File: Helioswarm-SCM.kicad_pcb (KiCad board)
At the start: 8 copper layers, 78 x 38 mm, 102 parts, among them J404 DB25_Female_MountingHoles, J405 DB15_Male_MountingHoles, U1 ASIC_JUICE

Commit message: Simplified schematic and reset(cleared) PCB
Signed-off-by: Alexis Jeandet <alexis.jeandet@member.fsf.org>
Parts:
- removed CX1, CX2, CX4, CY1, CY2, CY3, CZ1, CZ2, CZ3: 680n, Capacitor_SMD:C_1812_4532Metric_Pad1.30x3.40mm_HandSolder
- removed CX10, CX12, CY10, CY12, CZ10, CZ12: 221p, Capacitor_SMD:C_0603_1608Metric
- removed CX11, CX40, CY11, CY40, CZ11, CZ40: 220n, Capacitor_SMD:C_1206_3216Metric
- removed CX13, CY13, CZ13: 470nF, Capacitor_SMD:C_1210_3225Metric
- removed CX14, CY14, CZ14: 470n, Capacitor_SMD:C_1812_4532Metric_Pad1.30x3.40mm_HandSolder
- removed CX20, CX35, CX36, CX_SC1, CX_SC2, CY20, CY35, CY36, CY_SC1, CY_SC2, CZ20, CZ35, CZ36, CZ_SC1, CZ_SC2: *, Capacitor_SMD:C_0603_1608Metric
- removed CX42, CY42, CZ42: *, Capacitor_SMD:C_0805_2012Metric
- removed CX8, CY8, CZ8: 1n, Capacitor_SMD:C_0603_1608Metric
- removed CX_CR1, CY_CR1, CZ_CR1: 150pF, Capacitor_SMD:C_0603_1608Metric
- removed H1, H2: MountingHole, LibPersoNadj:MountingHole_4.2
- removed J404: DB25_Female_MountingHoles, LibPersoNadj:GMR7580-25S-1BPN
- removed J405: DB15_Male_MountingHoles, LibPersoNadj:GMR7580-15P-1BPN
- removed N_CFP64: Housing_Pad, TestPoint:TestPoint_Pad_2.0x2.0mm
- removed R1: 10k, Resistor_SMD:R_0603_1608Metric
- removed R40: c-c, Resistor_SMD:R_0805_2012Metric_Pad1.15x1.40mm_HandSolder
- removed RX10, RY10, RZ10: 22,1k, Resistor_SMD:R_0603_1608Metric
- removed RX12, RY12, RZ12: 44,2k, Resistor_SMD:R_0603_1608Metric
- removed RX14, RY14, RZ14: 400, Resistor_SMD:R_0603_1608Metric
- removed RX20, RY20, RZ20: 150k, Resistor_SMD:R_0805_2012Metric_Pad1.15x1.40mm_HandSolder
- removed RX30, RY30, RZ30: 7,68k, Resistor_SMD:R_0603_1608Metric
- removed RX31, RX33, RY31, RY33, RZ31, RZ33: 49,9k, Resistor_SMD:R_0603_1608Metric
- removed RX32, RX34, RY32, RY34, RZ32, RZ34: TBD, Resistor_SMD:R_0603_1608Metric
- removed RX35, RX36, RY35, RY36, RZ35, RZ36: 49,9, Resistor_SMD:R_0603_1608Metric
- removed RX40, RY40, RZ40: 750k, Resistor_SMD:R_1206_3216Metric
- removed RX41, RY41, RZ41: 24,9k, Resistor_SMD:R_0603_1608Metric
- removed RX42, RY42, RZ42: 42,2k, Resistor_SMD:R_0603_1608Metric
- removed RthB0: 1k, Resistor_SMD:R_0805_2012Metric_Pad1.15x1.40mm_HandSolder
- removed U1: ASIC_JUICE, LibPersoNadj:ASIC_Juice_CQFP-64
- added C201: *, Capacitor_SMD:C_0603_1608Metric, F.Cu at (110.7, 97.5)
- added C202: *, Capacitor_SMD:C_0603_1608Metric, F.Cu at (124.8, 90.1)
- added C203: *, Capacitor_SMD:C_0603_1608Metric, F.Cu at (116.3, 94.8)
- added C204: *, Capacitor_SMD:C_0603_1608Metric, F.Cu at (110.7, 100.1)
- added C205: *, Capacitor_SMD:C_0603_1608Metric, F.Cu at (120.8, 91.8)
- added C206: *, Capacitor_SMD:C_0603_1608Metric, F.Cu at (114.7, 97.5)
- added C207: 220n, Capacitor_SMD:C_1206_3216Metric, F.Cu at (111.5, 88.0)
- added C208: *, Capacitor_SMD:C_0805_2012Metric, F.Cu at (116.5, 92.1)
- added C212: 1n, Capacitor_SMD:C_0603_1608Metric, F.Cu at (126.0, 87.6)
- added C213: 221p, Capacitor_SMD:C_0603_1608Metric, F.Cu at (120.3, 94.8)
- added C214: 221p, Capacitor_SMD:C_0603_1608Metric, F.Cu at (114.7, 100.1)
- added C215: 220n, Capacitor_SMD:C_1206_3216Metric, F.Cu at (111.5, 91.3)
- added C216: 470nF, Capacitor_SMD:C_1210_3225Metric, F.Cu at (117.1, 88.4)
- added C301: *, Capacitor_SMD:C_0603_1608Metric, F.Cu at (110.7, 117.3)
- added C302: *, Capacitor_SMD:C_0603_1608Metric, F.Cu at (130.0, 106.4)
- added C303: *, Capacitor_SMD:C_0603_1608Metric, F.Cu at (116.3, 114.0)
- added C304: *, Capacitor_SMD:C_0603_1608Metric, F.Cu at (124.8, 108.9)
- added C305: *, Capacitor_SMD:C_0603_1608Metric, F.Cu at (132.8, 111.4)
- added C306: *, Capacitor_SMD:C_0603_1608Metric, F.Cu at (120.3, 112.8)
- added C307: 220n, Capacitor_SMD:C_1206_3216Metric, F.Cu at (117.1, 106.8)
- added C308: *, Capacitor_SMD:C_0805_2012Metric, F.Cu at (116.5, 110.0)
- added C312: 1n, Capacitor_SMD:C_0603_1608Metric, F.Cu at (114.7, 117.3)
- added C313: 221p, Capacitor_SMD:C_0603_1608Metric, F.Cu at (126.0, 106.4)
- added C314: 221p, Capacitor_SMD:C_0603_1608Metric, F.Cu at (120.8, 109.8)
- added C315: 220n, Capacitor_SMD:C_1206_3216Metric, F.Cu at (111.5, 111.1)
- added C316: 470nF, Capacitor_SMD:C_1210_3225Metric, F.Cu at (111.5, 107.3)
- added C401: *, Capacitor_SMD:C_0603_1608Metric, F.Cu at (145.9, 97.5)
- added C402: *, Capacitor_SMD:C_0603_1608Metric, F.Cu at (151.9, 91.8)
- added C403: *, Capacitor_SMD:C_0603_1608Metric, F.Cu at (141.8, 100.1)
- added C404: *, Capacitor_SMD:C_0603_1608Metric, F.Cu at (147.5, 94.8)
- added C405: *, Capacitor_SMD:C_0603_1608Metric, F.Cu at (141.8, 97.5)
- added C406: *, Capacitor_SMD:C_0603_1608Metric, F.Cu at (157.9, 95.1)
- added C407: 220n, Capacitor_SMD:C_1206_3216Metric, F.Cu at (142.7, 88.0)
- added C408: *, Capacitor_SMD:C_0805_2012Metric, F.Cu at (147.7, 92.1)
- added C412: 1n, Capacitor_SMD:C_0603_1608Metric, F.Cu at (157.2, 87.6)
- added C413: 221p, Capacitor_SMD:C_0603_1608Metric, F.Cu at (151.5, 94.8)
- added C414: 221p, Capacitor_SMD:C_0603_1608Metric, F.Cu at (145.9, 100.1)
- added C415: 220n, Capacitor_SMD:C_1206_3216Metric, F.Cu at (142.7, 91.3)
- added C416: 470nF, Capacitor_SMD:C_1210_3225Metric, F.Cu at (148.3, 88.4)
- added H101: MountingHole, LibPersoNadj:MountingHole_4.2, F.Cu at (201.0, 98.5)
- added H102: MountingHole, LibPersoNadj:MountingHole_4.2, F.Cu at (194.8, 109.5)
- added J101: DB15_Male_MountingHoles, LibPersoNadj:GMR7580-15P-1BPN, F.Cu at (176.4, 110.1)
- added J102: DB25_Female_MountingHoles, LibPersoNadj:GMR7580-25S-1BPN, F.Cu at (179.5, 99.1)
- added N_CFP101: Housing_Pad, TestPoint:TestPoint_Pad_2.0x2.0mm, F.Cu at (141.9, 107.2)
- added R101: 10k, Resistor_SMD:R_0603_1608Metric, F.Cu at (145.9, 106.4)
- added R202: 49,9, Resistor_SMD:R_0603_1608Metric, F.Cu at (122.0, 87.6)
- added R203: 7,68k, Resistor_SMD:R_0603_1608Metric, F.Cu at (118.7, 97.3)
- added R204: 49,9k, Resistor_SMD:R_0603_1608Metric, F.Cu at (130.0, 87.6)
- added R205: TBD, Resistor_SMD:R_0603_1608Metric, F.Cu at (124.8, 92.6)
- added R206: 49,9, Resistor_SMD:R_0603_1608Metric, F.Cu at (118.7, 99.8)
- added R207: TBD, Resistor_SMD:R_0603_1608Metric, F.Cu at (128.8, 90.1)
- added R208: 750k, Resistor_SMD:R_1206_3216Metric, F.Cu at (111.5, 94.6)
- added R209: 42,2k, Resistor_SMD:R_0603_1608Metric, F.Cu at (122.7, 97.3)
- added R210: 24,9k, Resistor_SMD:R_0603_1608Metric, F.Cu at (134.0, 87.6)
- added R211: 49,9k, Resistor_SMD:R_0603_1608Metric, F.Cu at (128.8, 92.6)
- added R212: 400, Resistor_SMD:R_0603_1608Metric, F.Cu at (122.7, 99.8)
- added R213: 22,1k, Resistor_SMD:R_0603_1608Metric, F.Cu at (132.8, 90.1)
- added R214: 44,2k, Resistor_SMD:R_0603_1608Metric, F.Cu at (126.7, 95.1)
- added R302: 49,9, Resistor_SMD:R_0603_1608Metric, F.Cu at (124.8, 111.4)
- added R303: 7,68k, Resistor_SMD:R_0603_1608Metric, F.Cu at (122.7, 119.0)
- added R304: 49,9k, Resistor_SMD:R_0603_1608Metric, F.Cu at (128.3, 114.0)
- added R305: TBD, Resistor_SMD:R_0603_1608Metric, F.Cu at (124.3, 116.5)
- added R306: 49,9, Resistor_SMD:R_0603_1608Metric, F.Cu at (132.8, 108.9)
- added R307: TBD, Resistor_SMD:R_0603_1608Metric, F.Cu at (128.8, 111.4)
- added R308: 750k, Resistor_SMD:R_1206_3216Metric, F.Cu at (111.5, 114.4)
- added R309: 42,2k, Resistor_SMD:R_0603_1608Metric, F.Cu at (134.0, 106.4)
- added R310: 24,9k, Resistor_SMD:R_0603_1608Metric, F.Cu at (124.3, 114.0)
- added R311: 49,9k, Resistor_SMD:R_0603_1608Metric, F.Cu at (118.7, 117.8)
- added R312: 400, Resistor_SMD:R_0603_1608Metric, F.Cu at (128.8, 108.9)
- added R313: 22,1k, Resistor_SMD:R_0603_1608Metric, F.Cu at (120.3, 115.3)
- added R314: 44,2k, Resistor_SMD:R_0603_1608Metric, F.Cu at (122.0, 106.4)
- added R402: 49,9, Resistor_SMD:R_0603_1608Metric, F.Cu at (153.1, 87.6)
- added R403: 7,68k, Resistor_SMD:R_0603_1608Metric, F.Cu at (149.9, 97.3)
- added R404: 49,9k, Resistor_SMD:R_0603_1608Metric, F.Cu at (161.2, 87.6)
- added R405: TBD, Resistor_SMD:R_0603_1608Metric, F.Cu at (156.0, 92.6)
- added R406: 49,9, Resistor_SMD:R_0603_1608Metric, F.Cu at (149.9, 99.8)
- added R407: TBD, Resistor_SMD:R_0603_1608Metric, F.Cu at (160.0, 90.1)
- added R408: 750k, Resistor_SMD:R_1206_3216Metric, F.Cu at (142.6, 94.6)
- added R409: 42,2k, Resistor_SMD:R_0603_1608Metric, F.Cu at (153.9, 97.3)
- added R410: 24,9k, Resistor_SMD:R_0603_1608Metric, F.Cu at (165.2, 87.6)
- added R411: 49,9k, Resistor_SMD:R_0603_1608Metric, F.Cu at (160.0, 92.6)
- added R412: 400, Resistor_SMD:R_0603_1608Metric, F.Cu at (153.9, 99.8)
- added R413: 22,1k, Resistor_SMD:R_0603_1608Metric, F.Cu at (164.0, 90.1)
- added R414: 44,2k, Resistor_SMD:R_0603_1608Metric, F.Cu at (156.0, 90.1)
- added U201: ASIC_JUICE, LibPersoNadj:ASIC_Juice_CQFP-64, F.Cu at (172.5, 132.7)
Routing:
- net /Sz: track 71.6 -> 0.00 mm, vias 1 -> 0
- net /+6V_C: track 68.9 -> 0.00 mm, vias 2 -> 0
- net /CAL: track 66.1 -> 0.00 mm, vias 2 -> 0
- net /M_X: track 62.2 -> 0.00 mm, vias 2 -> 0
- net /+6V_B: track 61.7 -> 0.00 mm, vias 2 -> 0
- net /+6V_A: track 55.1 -> 0.00 mm, vias 2 -> 0
- net /M_Y: track 54.2 -> 0.00 mm, vias 2 -> 0
- net /RTNz: track 52.7 -> 0.00 mm, vias 1 -> 0
- net /RTNx: track 50.8 -> 0.00 mm, vias 1 -> 0
- net GND: track 47.7 -> 0.00 mm, vias 38 -> 0
- net /AsicFM/VDD_Y: track 44.0 -> 0.00 mm, vias 3 -> 0
- net /RTNy: track 42.5 -> 0.00 mm, vias 1 -> 0
- net /Sx: track 39.3 -> 0.00 mm, vias 1 -> 0
- net /AsicFM/VDD_X: track 35.1 -> 0.00 mm, vias 2 -> 0
- net /AsicFM/In2P_Y: track 35.0 -> 0.00 mm, vias 2 -> 0
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- removed copper zone on B.Cu, net GND
- removed copper zone on F.Cu, net GND
- removed copper zone on In1.Cu, net GND
- removed copper zone on In2.Cu, net GND
- removed copper zone on In3.Cu, net GND
- removed copper zone on In4.Cu, net GND
- removed copper zone on In5.Cu, net GND
- removed copper zone on In6.Cu, net GND
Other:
- board outline removed

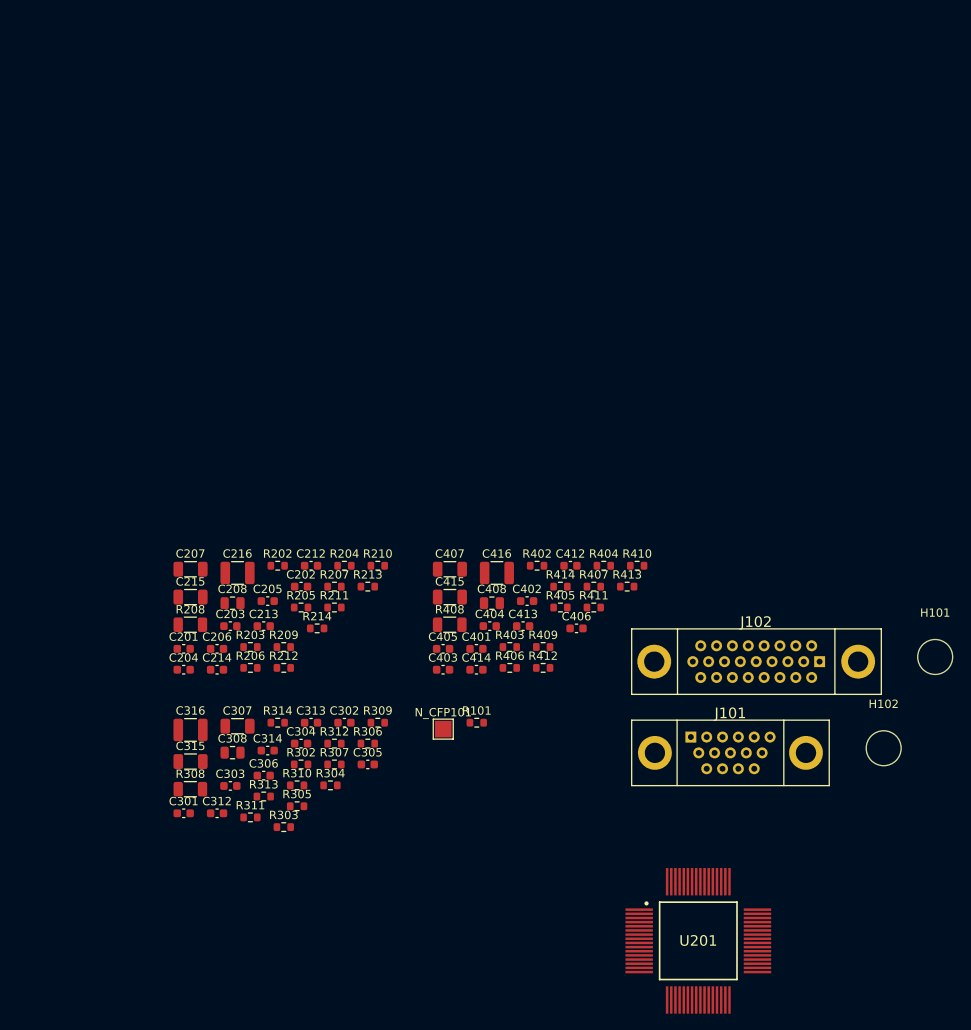
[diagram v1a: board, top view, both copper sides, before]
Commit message: Improved schematic net naming and started layout
Signed-off-by: Alexis Jeandet <alexis.jeandet@member.fsf.org>
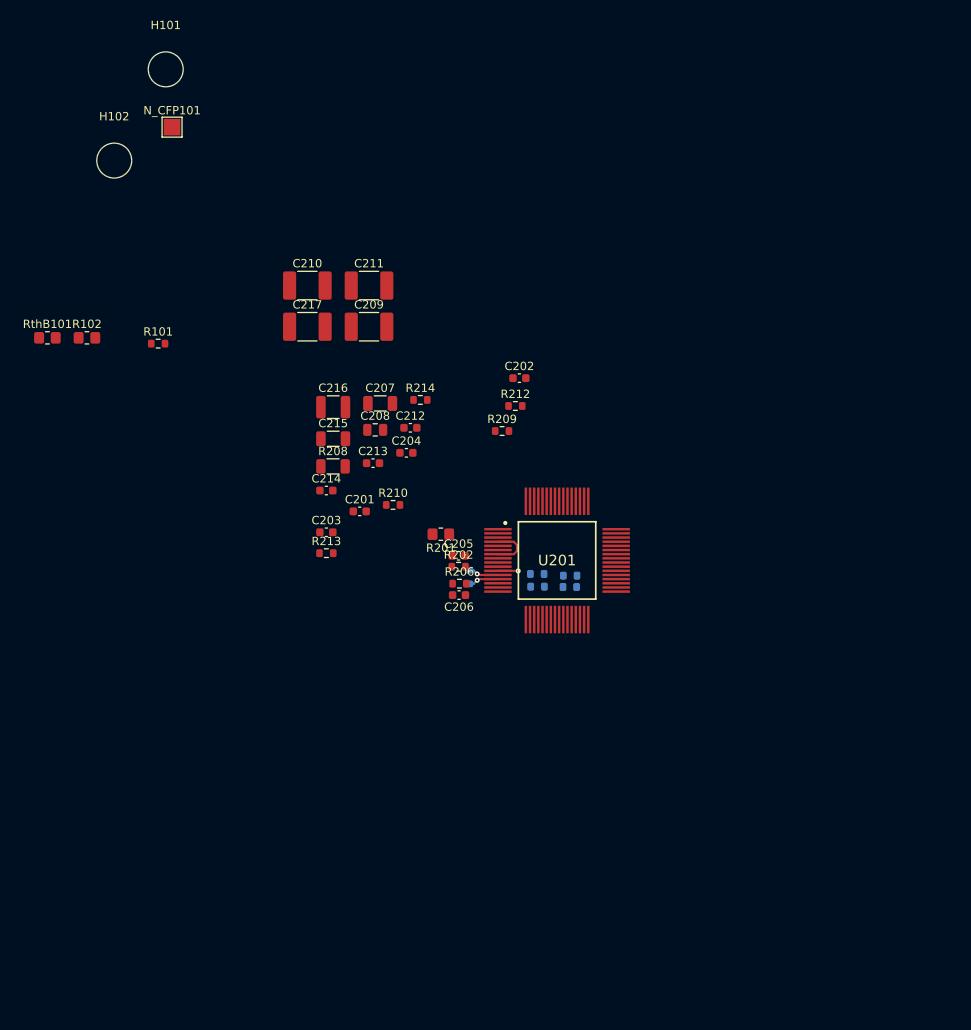
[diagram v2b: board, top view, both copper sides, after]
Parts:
- removed C301, C302, C303, C304, C305, C306, C401, C402, C403, C404, C405, C406: *, Capacitor_SMD:C_0603_1608Metric
- removed C307, C315, C407, C415: 220n, Capacitor_SMD:C_1206_3216Metric
- removed C308, C408: *, Capacitor_SMD:C_0805_2012Metric
- removed C312, C412: 1n, Capacitor_SMD:C_0603_1608Metric
- removed C313, C314, C413, C414: 221p, Capacitor_SMD:C_0603_1608Metric
- removed C316, C416: 470nF, Capacitor_SMD:C_1210_3225Metric
- removed J101: DB15_Male_MountingHoles, LibPersoNadj:GMR7580-15P-1BPN
- removed J102: DB25_Female_MountingHoles, LibPersoNadj:GMR7580-25S-1BPN
- removed R302, R306, R402, R406: 49,9, Resistor_SMD:R_0603_1608Metric
- removed R303, R403: 7,68k, Resistor_SMD:R_0603_1608Metric
- removed R304, R311, R404, R411: 49,9k, Resistor_SMD:R_0603_1608Metric
- removed R305, R307, R405, R407: TBD, Resistor_SMD:R_0603_1608Metric
- removed R308, R408: 750k, Resistor_SMD:R_1206_3216Metric
- removed R309, R409: 42,2k, Resistor_SMD:R_0603_1608Metric
- removed R310, R410: 24,9k, Resistor_SMD:R_0603_1608Metric
- removed R312, R412: 400, Resistor_SMD:R_0603_1608Metric
- removed R313, R413: 22,1k, Resistor_SMD:R_0603_1608Metric
- removed R314, R414: 44,2k, Resistor_SMD:R_0603_1608Metric
- added C209: 680n, Capacitor_SMD:C_1812_4532Metric_Pad1.57x3.40mm_HandSolder, F.Cu at (132.9, 58.8)
- added C210: 680n, Capacitor_SMD:C_1812_4532Metric_Pad1.57x3.40mm_HandSolder, F.Cu at (125.5, 53.9)
- added C211: 680n, Capacitor_SMD:C_1812_4532Metric_Pad1.57x3.40mm_HandSolder, F.Cu at (132.9, 53.9)
- added C217: 470n, Capacitor_SMD:C_1812_4532Metric_Pad1.57x3.40mm_HandSolder, F.Cu at (125.5, 58.8)
- added R102: c-c, Resistor_SMD:R_0805_2012Metric_Pad1.20x1.40mm_HandSolder, F.Cu at (99.0, 60.2)
- added R201: 150k, Resistor_SMD:R_0805_2012Metric_Pad1.20x1.40mm_HandSolder, F.Cu at (141.6, 83.8)
- added RthB101: 1k, Resistor_SMD:R_0805_2012Metric_Pad1.20x1.40mm_HandSolder, F.Cu at (94.3, 60.2)
- R203, R204, R205, R207, R211: moved to B.Cu
- moved H101 116.4 mm to (108.5, 27.9)
- moved H102 116.4 mm to (102.3, 38.9)
- moved N_CFP101 79.4 mm to (109.3, 34.8)
- moved R101 59.5 mm to (107.6, 60.9)
- moved U201 48.8 mm to (155.5, 86.9)
- moved R212 42.0 mm to (150.5, 68.4)
- moved C204 37.4 mm to (137.4, 74.0)
- moved R209 36.9 mm to (148.9, 71.4)
- moved C202 36.3 mm to (151.0, 65.0)
- moved C207 30.3 mm to (134.3, 68.0)
- moved R214 30.1 mm to (139.1, 67.6)
- moved C206 29.8 mm to (143.8, 91.1), turned to 180 degrees
- moved R205 28.7 mm to (153.2, 88.5)
- moved R211 28.4 mm to (157.1, 90.1), turned to 180 degrees
- moved R207 28.4 mm to (157.1, 88.7)
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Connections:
- net /+6V_A renamed /VDD_X
- net /ASIC_X_Channel/CAL_Gain renamed Net-(R210-Pad1)
- net /ASIC_X_Channel/CAL_In renamed Net-(C207-Pad1)
- net /ASIC_X_Channel/CAL_Out renamed Net-(C208-Pad1)
- net /ASIC_X_Channel/Gain_Out2_N renamed Net-(R203-Pad2)
- net /ASIC_X_Channel/Gain_Out2_P renamed Net-(R203-Pad1)
- net /ASIC_X_Channel/In2N renamed Net-(R205-Pad1)
- net /ASIC_X_Channel/Out2_NInv renamed Net-(R202-Pad2)
- net /ASIC_X_Channel/Out2_inv renamed Net-(R206-Pad2)
- net /ASIC_X_Channel/Regu_Bias_LNA renamed Net-(C213-Pad2)
- net /ASIC_X_Channel/Regu_VDD renamed Net-(C214-Pad2)
- net /ASIC_X_Channel/V_Bias_LNA renamed Net-(C213-Pad1)
- net /Sx renamed /SX+
- C201 pad 1: /CR_X -> /ASIC_X_Channel/CR
- C203 pad 1: /B_X -> /M_X
- C203 pad 2: /M_X -> /SCM_X
- C204 pad 1: /B_X -> /M_X
- C204 pad 2: /M_X -> /SCM_X
- C206 pad 1: /RTNx -> GND
- C206 pad 2: GND -> /SX-
- R206 pad 1: /RTNx -> /SX-
- U201 pad 19: /ASIC_Z_Channel/Out2_inv -> Net-(R406-Pad2)
- U201 pad 20: /ASIC_Z_Channel/Gain_Out2_P -> Net-(R403-Pad1)
- U201 pad 21: /ASIC_Z_Channel/Gain_Out2_N -> Net-(R403-Pad2)
- U201 pad 22: /ASIC_Z_Channel/In2N -> Net-(R405-Pad1)
- U201 pad 23: /ASIC_Z_Channel/Out2_NInv -> Net-(R402-Pad2)
- U201 pad 28: /B_Z -> /SCM_Z
- U201 pad 30: /ASIC_Z_Channel/Regu_Bias_LNA -> Net-(C413-Pad2)
- U201 pad 31: /ASIC_Z_Channel/Regu_VDD -> Net-(C414-Pad2)
- U201 pad 33: /ASIC_Z_Channel/V_Bias_LNA -> Net-(C413-Pad1)
- U201 pad 35: /ASIC_Z_Channel/CAL_In -> Net-(C407-Pad1)
- U201 pad 36: /ASIC_Z_Channel/CAL_Out -> Net-(C408-Pad1)
- U201 pad 37: /ASIC_Z_Channel/CAL_Gain -> Net-(R410-Pad1)
- U201 pad 38: /+6V_C -> /VDD_Z
- U201 pad 39: /+6V_B -> /VDD_Y
- U201 pad 40: /ASIC_Y_Channel/CAL_Gain -> Net-(R310-Pad1)
- U201 pad 41: /ASIC_Y_Channel/CAL_Out -> Net-(C308-Pad1)
- U201 pad 42: /ASIC_Y_Channel/CAL_In -> Net-(C307-Pad1)
- U201 pad 43: /ASIC_Y_Channel/Regu_VDD -> Net-(C314-Pad2)
- U201 pad 46: /ASIC_Y_Channel/Regu_Bias_LNA -> Net-(C313-Pad2)
- U201 pad 47: /ASIC_Y_Channel/V_Bias_LNA -> Net-(C313-Pad1)
- U201 pad 49: /ASIC_Y_Channel/Out2_NInv -> Net-(R302-Pad2)
- U201 pad 5: /B_X -> /SCM_X
- U201 pad 50: /ASIC_Y_Channel/Gain_Out2_P -> Net-(R303-Pad1)
- U201 pad 52: /B_Y -> /SCM_Y
- U201 pad 55: /ASIC_Y_Channel/Gain_Out2_N -> Net-(R303-Pad2)
- U201 pad 56: /ASIC_Y_Channel/In2N -> Net-(R305-Pad1)
- U201 pad 57: /ASIC_Y_Channel/Out2_inv -> Net-(R306-Pad2)
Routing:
- net /ASIC_X_Channel/In2P: track 0.00 -> 5.63 mm
- net Net-(R203-Pad2): track 0.00 -> 3.72 mm, vias 0 -> 1
- net Net-(R203-Pad1): track 0.00 -> 3.69 mm, vias 0 -> 1
- net Net-(R205-Pad1): track 0.00 -> 2.44 mm, vias 0 -> 1
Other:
- rule trace_min: 0.2 -> 0.15
- rule via_min_drill: 0.3 -> 0.25

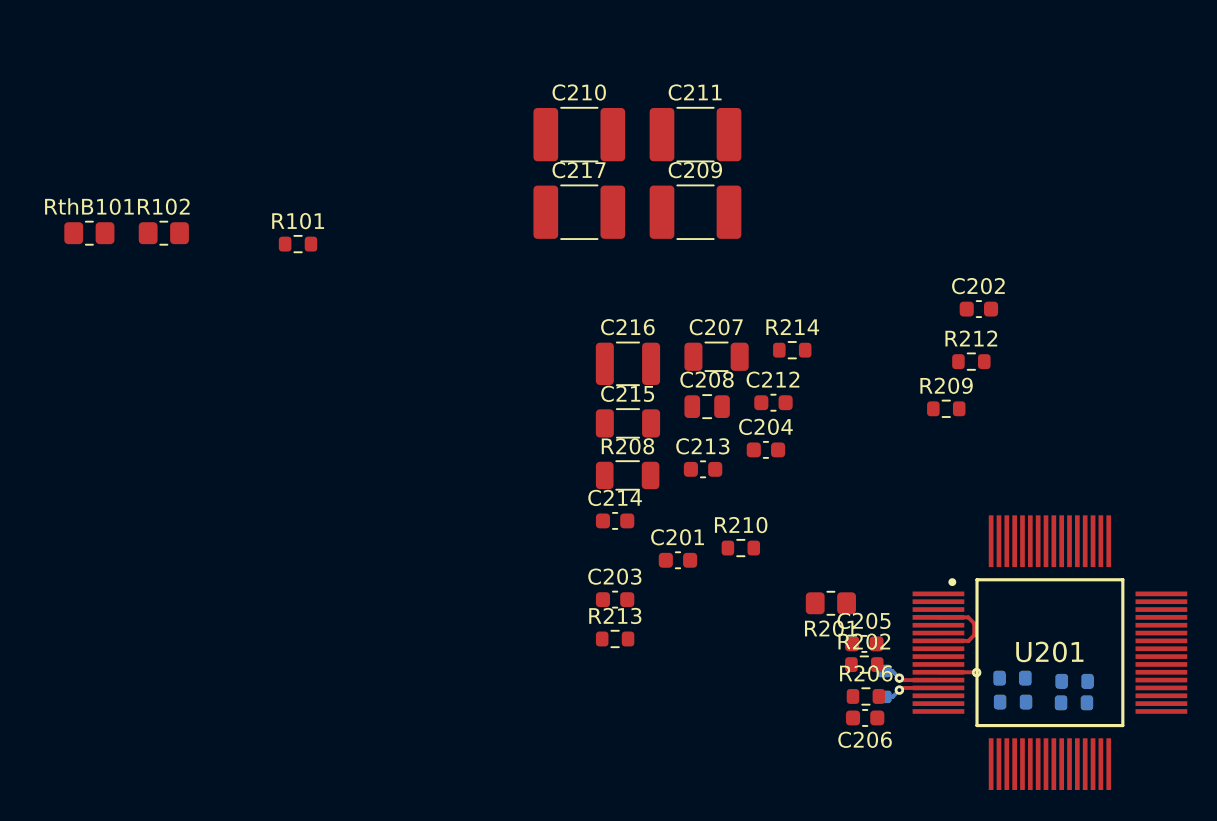
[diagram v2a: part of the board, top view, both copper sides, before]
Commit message: Fixed SCH mistakes and Layout WIP
Signed-off-by: Alexis Jeandet <alexis.jeandet@member.fsf.org>
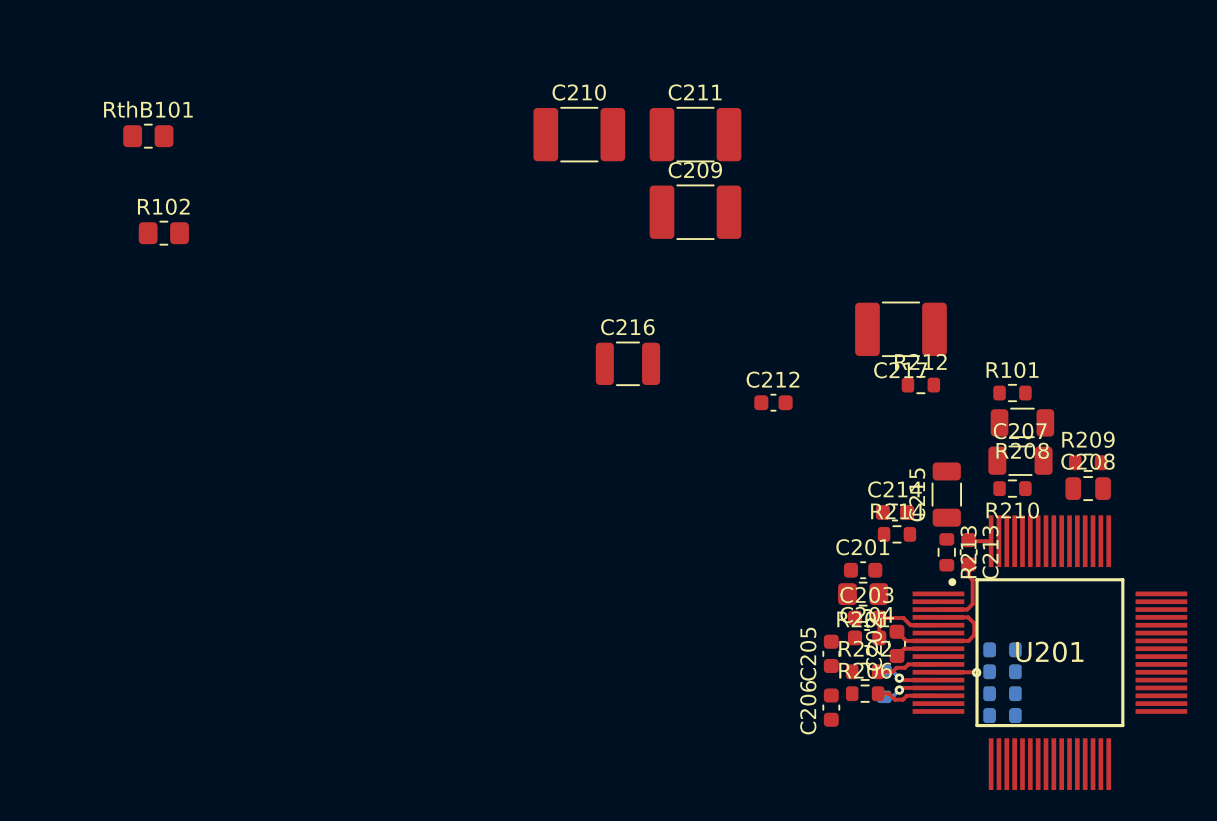
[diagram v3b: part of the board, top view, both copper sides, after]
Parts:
- moved R101 46.5 mm to (153.2, 70.4)
- moved R208 25.4 mm to (153.8, 72.3), turned to 180 degrees
- moved C208 24.9 mm to (158.0, 76.5)
- moved C202 22.0 mm to (145.8, 86.4), turned to 90 degrees
- moved R213 21.9 mm to (149.0, 80.5), turned to 270 degrees
- moved C217 21.8 mm to (146.1, 66.3), turned to 180 degrees
- moved C215 20.8 mm to (149.0, 76.8), turned to 90 degrees
- moved C207 20.5 mm to (153.7, 74.7)
- moved C214 17.9 mm to (145.7, 78.0)
- moved C213 17.7 mm to (150.4, 80.5), turned to 270 degrees
- moved R210 17.7 mm to (153.2, 76.5), turned to 180 degrees
- moved C203 16.1 mm to (143.9, 84.7)
- moved C204 13.6 mm to (143.9, 86.0)
- moved R214 13.5 mm to (145.8, 79.4)
- moved C201 11.8 mm to (143.6, 81.7)
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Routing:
- net /SCM_X: track 0.00 -> 5.23 mm
- net Net-(C213-Pad2): track 0.00 -> 4.96 mm
- net Net-(R206-Pad2): track 0.00 -> 4.11 mm
- net Net-(R202-Pad2): track 0.00 -> 4.05 mm
- net /ASIC_X_Channel/In2P: track 5.63 -> 8.51 mm
- net /ASIC_X_Channel/In1N: track 0.00 -> 2.84 mm
- net Net-(C213-Pad1): track 0.00 -> 1.46 mm
